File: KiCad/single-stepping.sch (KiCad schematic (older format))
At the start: 8 parts, among them SW1 SW_PUSH_SMALL, U1 4013, U2 74LS00, X1 OSCILLATOR

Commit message: add single-stepped CPU symbol to schema, with LED to blink
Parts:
- added D1: LED, symbol cpu-board-rescue:LED
- added R2: 330, symbol cpu-board-rescue:R
- added U4: 68008D, symbol CPU_NXP_68000:68008D
- gave numbers to parts that had none: 1
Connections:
- net +5V: now also U4.13 (VCC), U4.33 (BR), U4.36 (HALT), U4.37 (RESET), U4.39 (VPA), U4.40 (BERR), U4.41 (IPL1), U4.42 (IPL0/2)
- net DTACK: now also U4.31 (DTACK)
- net GND: now also R2.1, U4.15 (GND), U4.20 (D7), U4.21 (D6), U4.22 (D5), U4.23 (D4), U4.24 (D3), U4.25 (D2), U4.26 (D1), U4.27 (D0), U4.35 (GND)
- net CLK: now reaches U1.11 (C), U1.3 (C), X1.5 (OUT)
- net CLK: now also U4.34 (CLK)
- new net: D1.1 (A), U4.46 (A0)
- new net: D1.2 (K), R2.2
- no-connect marks 3 -> 30

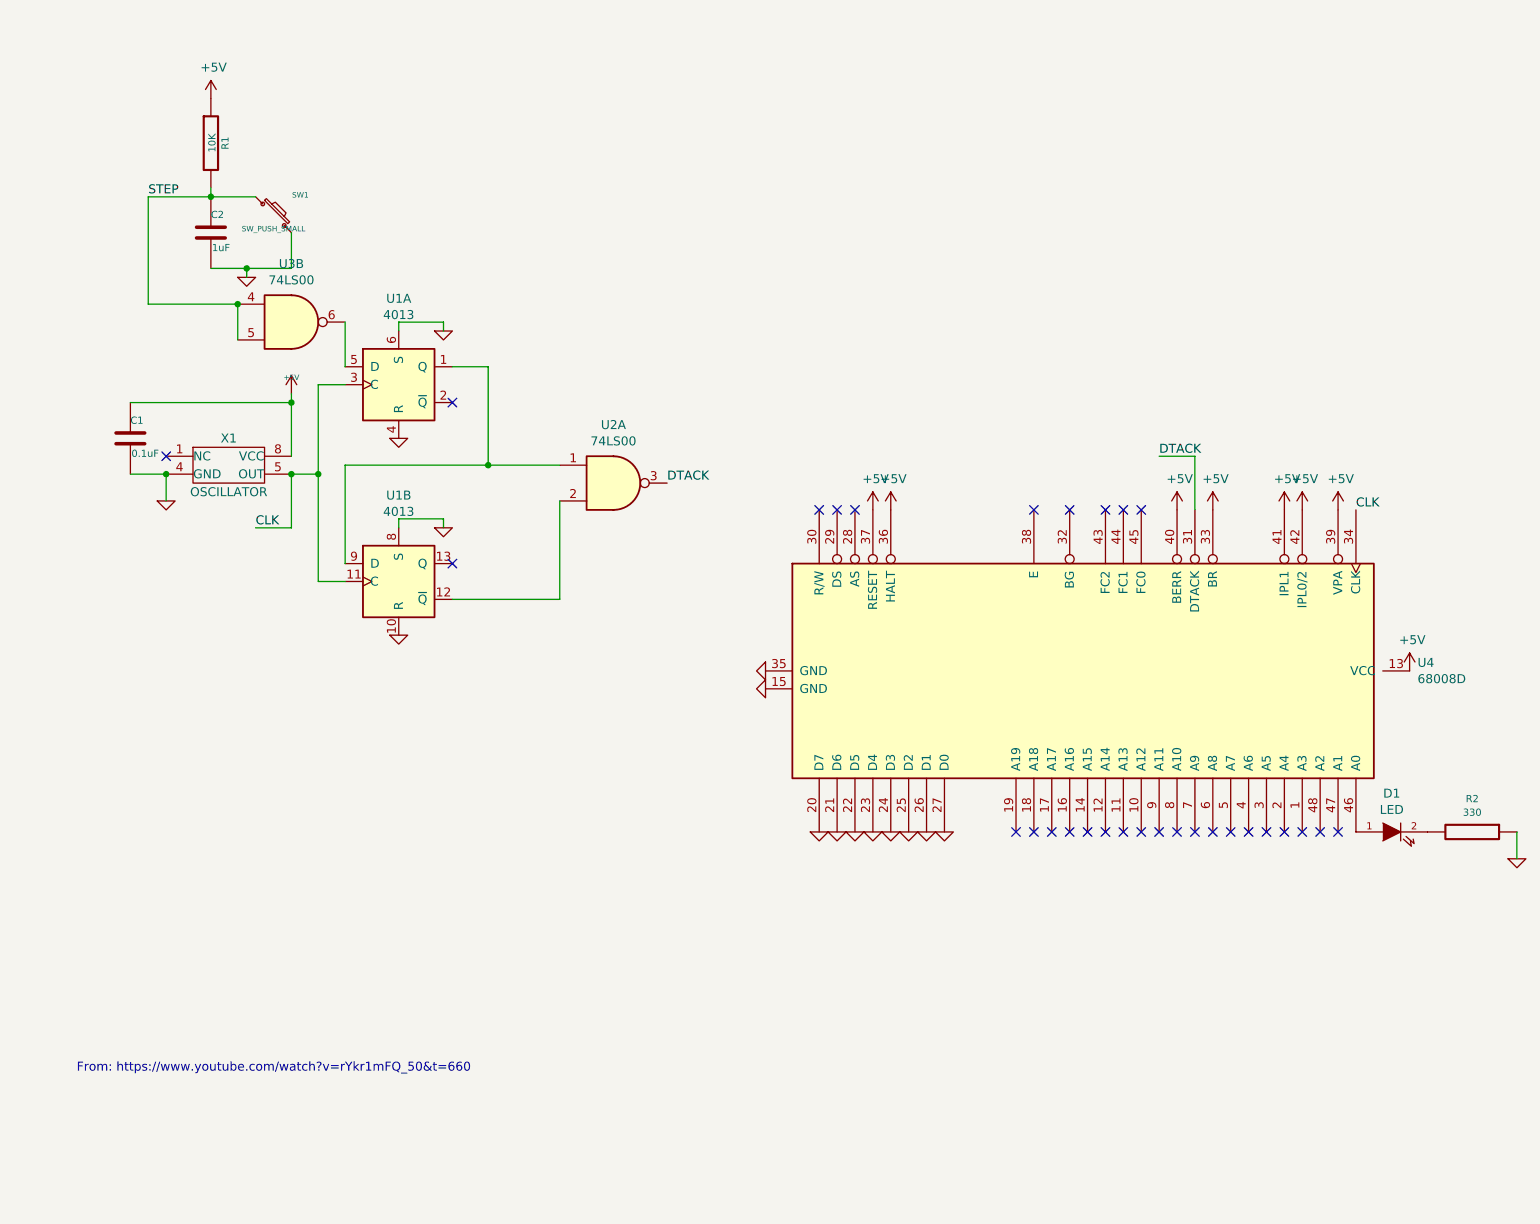
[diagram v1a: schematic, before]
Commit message: fix halt and error line high to pulled high, add power-up reset circuitry
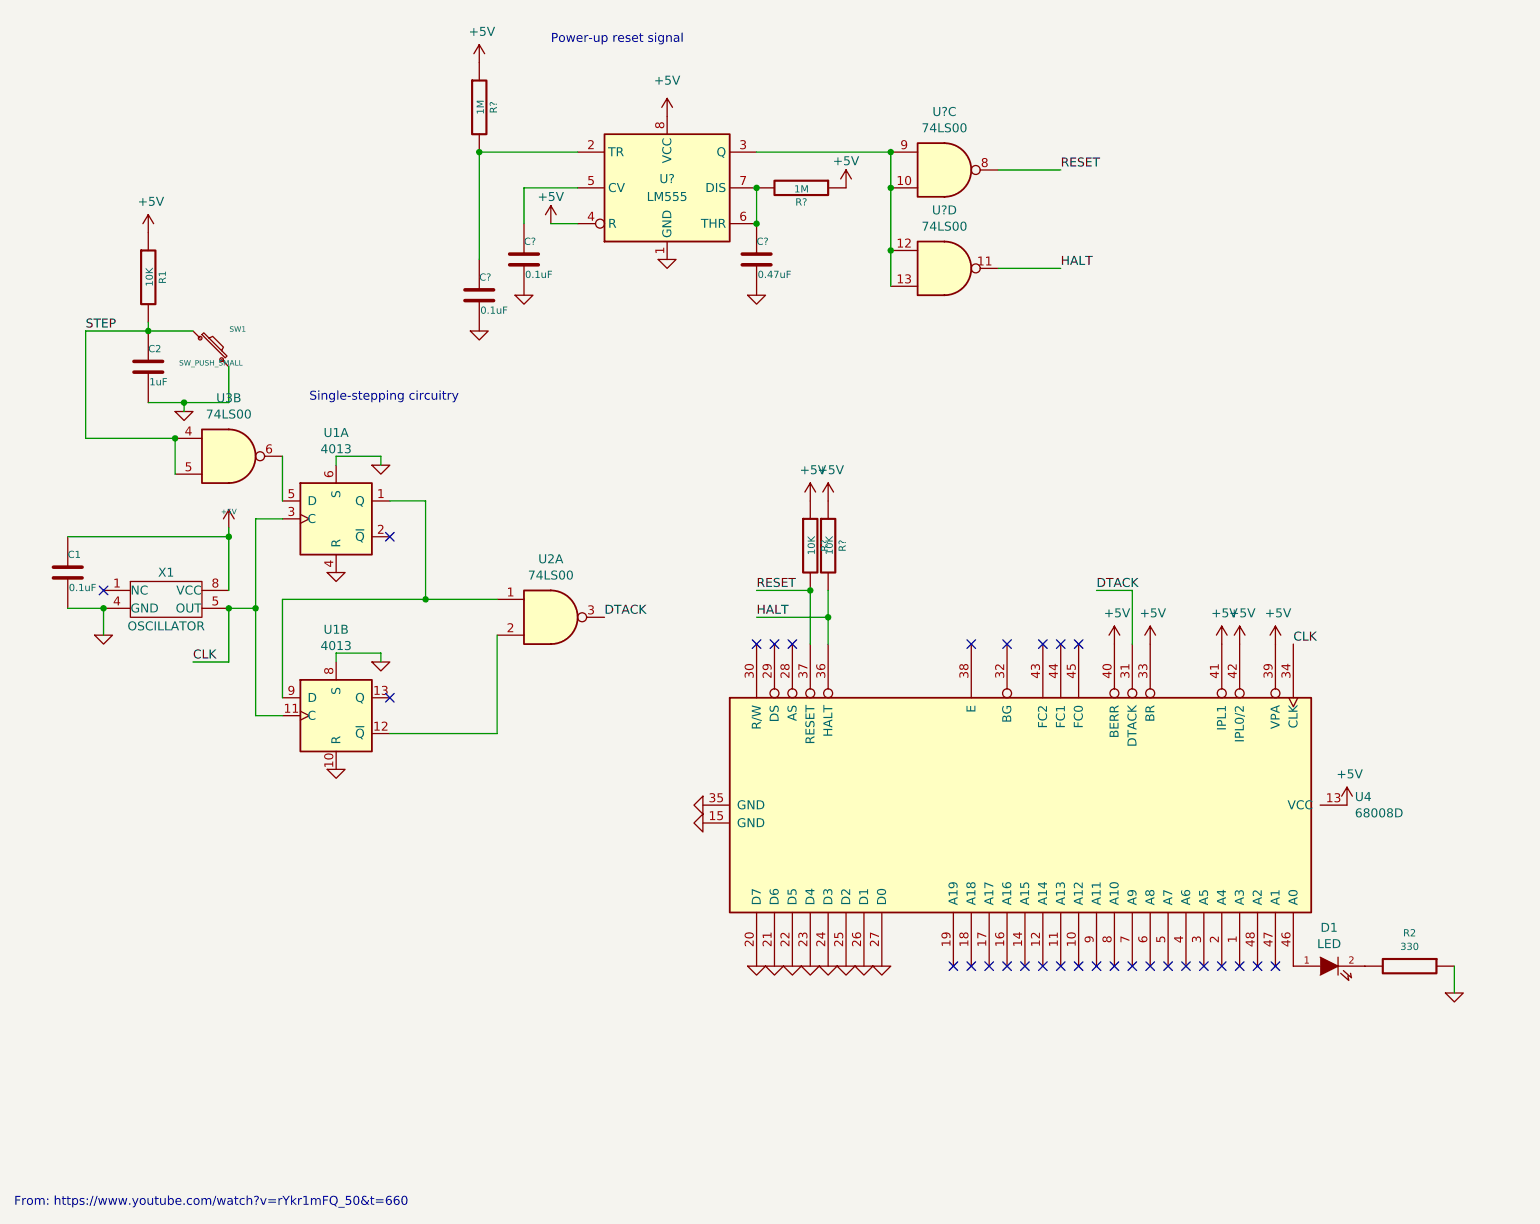
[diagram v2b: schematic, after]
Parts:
- added C? (x2): 0.1uF, Discret:C1, symbol cpu-board-rescue:C
- added C?: 0.47uF, Discret:C1, symbol cpu-board-rescue:C
- added R? (x2): 10K, Discret:R3-5, symbol cpu-board-rescue:R
- added R? (x2): 1M, Discret:R3-5, symbol cpu-board-rescue:R
- added U?: LM555, symbol Timer:LM555
- added U? (x2): 74LS00, symbol 74xx:74LS00
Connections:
- net +5V: now also R?.1, R?.1, R?.1, R?.1, U?.4 (R), U?.8 (VCC); no longer U4.36 (HALT), U4.37 (RESET)
- net GND: now also C?.2, C?.2, C?.2, U?.1 (GND)
- new net: C?.1, R?.2, U?.2 (TR)
- new net: U?.10, U?.12, U?.13, U?.3 (Q), U?.9
- new net: C?.1, U?.5 (CV)
- new net: C?.1, R?.2, U?.6 (THR), U?.7 (DIS)
- new net HALT: R?.2, U4.36 (HALT), U?.11
- new net RESET: R?.2, U4.37 (RESET), U?.8
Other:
- note added: "Power-up reset signal"
- note added: "Single-stepping circuitry"
- moved on the sheet: C1, C2, D1, R1, R2, SW1, U1A, U1B, U2A, U3B, U4, X1

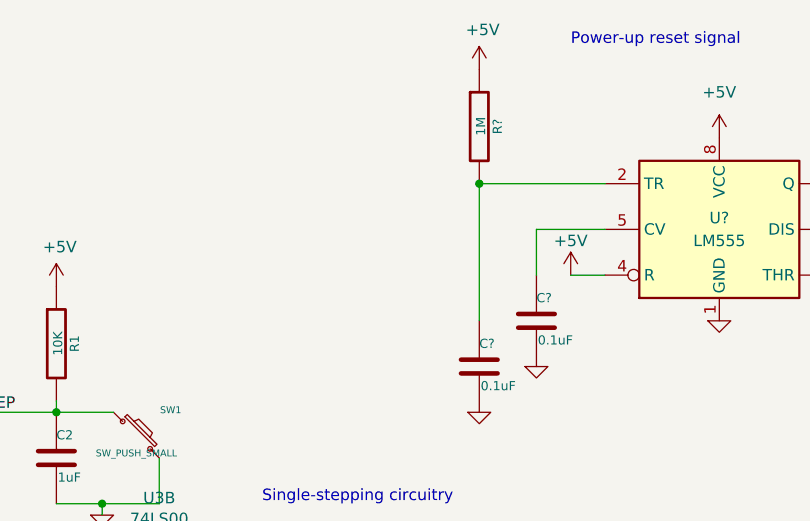
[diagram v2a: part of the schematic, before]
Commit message: Add reset switch
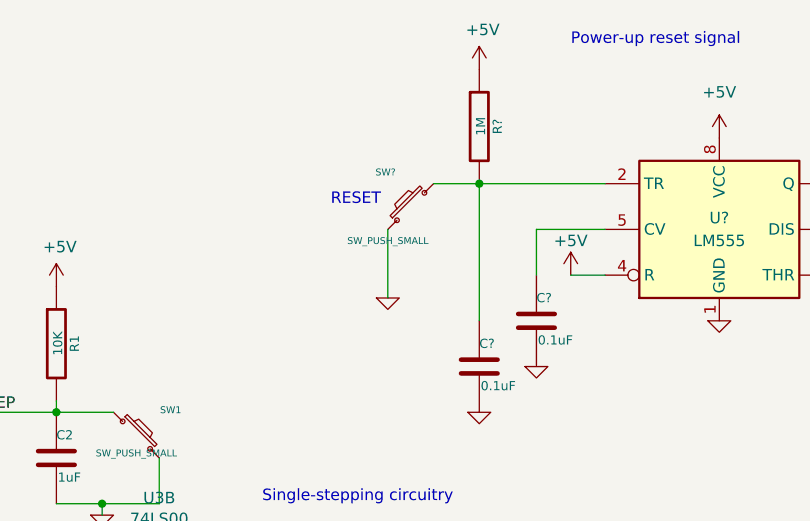
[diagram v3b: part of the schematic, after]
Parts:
- added SW?: SW_PUSH_SMALL, Discret:SW_PUSH_SMALL, symbol cpu-board-rescue:SW_PUSH_SMALL
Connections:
- net GND: now also SW?.1
- net at C?.1, R?.2, U?.2 (TR): now also SW?.2
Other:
- note added: "RESET"
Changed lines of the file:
@@
 Text Notes 2750 2850 0    50   ~ 0
 Single-stepping circuitry
+$Comp
+L cpu-board-rescue:SW_PUSH_SMALL SW?
+U 1 1 5E6E0874
+P 3400 1550
+F 0 "SW?" V 3550 1660 30  0000 C CNN
+F 1 "SW_PUSH_SMALL" V 3250 1650 30  0000 C CNN
+F 2 "Discret:SW_PUSH_SMALL" H 3400 1550 60  0001 C CNN
+F 3 "" H 3400 1550 60  0000 C CNN
+	1    3400 1550
+	0    -1   -1   0
+$EndComp
+Wire Wire Line
+	3500 1450 3700 1450
+Wire Wire Line
+	3300 1650 3300 1950
+$Comp
+L cpu-board-rescue:GND #PWR?
+U 1 1 5E6E4E67
+P 3300 1950
+F 0 "#PWR?" H 3300 1950 30  0001 C CNN
+F 1 "GND" H 3300 1880 30  0001 C CNN
+F 2 "" H 3300 1950 60  0000 C CNN
+F 3 "" H 3300 1950 60  0000 C CNN
+	1    3300 1950
+	1    0    0    -1
+$EndComp
+Text Notes 3050 1550 0    50   ~ 0
+RESET
 $EndSCHEMATC

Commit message: re-order pin configuration, trigger on DTACK
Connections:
- net DTACK renamed ~DTACK
- net HALT renamed ~HALT
- net RESET renamed ~RESET
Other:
- note added: "Power-up reset signal\nAdapted from Jeff Tranter's https://github.com/jefftranter/68000/blob/master/TS2/v2.1/page1.sch"
- note removed: "Power-up reset signal"
- moved on the sheet: C?, R?, SW?
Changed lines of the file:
@@
 NoConn ~ 3200 4500
 Text Label 4400 4050 0    50   ~ 0
-DTACK
+~DTACK
 $Comp
 L cpu-board-rescue:GND #PWR05
@@
 	7350 3900 7150 3900
 Text Label 7150 3900 0    50   ~ 0
-DTACK
+~DTACK
 $Comp
 L power:+5V #PWR023
@@
 	5650 4050 5650 3900
 Text Label 5250 3900 0    50   ~ 0
-RESET
+~RESET
 Text Label 5250 4050 0    50   ~ 0
-HALT
+~HALT
 $Comp
 L Timer:LM555 U?
@@
 L cpu-board-rescue:R R?
 U 1 1 5E6B3594
-P 3700 1200
-F 0 "R?" V 3780 1200 40  0000 C CNN
-F 1 "1M" V 3707 1201 40  0000 C CNN
-F 2 "Discret:R3-5" V 3630 1200 30  0001 C CNN
-F 3 "" H 3700 1200 30  0000 C CNN
-	1    3700 1200
+P 3600 1200
+F 0 "R?" V 3680 1200 40  0000 C CNN
+F 1 "1M" V 3607 1201 40  0000 C CNN
+F 2 "Discret:R3-5" V 3530 1200 30  0001 C CNN
+F 3 "" H 3600 1200 30  0000 C CNN
+	1    3600 1200
 	1    0    0    -1
 $EndComp
@@
 L cpu-board-rescue:C C?
 U 1 1 5E6B3B78
-P 3700 2250
-F 0 "C?" H 3700 2350 40  0000 L CNN
-F 1 "0.1uF" H 3706 2165 40  0000 L CNN
-F 2 "Discret:C1" H 3738 2100 30  0001 C CNN
-F 3 "" H 3700 2250 60  0000 C CNN
-	1    3700 2250
+P 3600 2050
+F 0 "C?" H 3600 2150 40  0000 L CNN
+F 1 "0.1uF" H 3606 1965 40  0000 L CNN
+F 2 "Discret:C1" H 3638 1900 30  0001 C CNN
+F 3 "" H 3600 2050 60  0000 C CNN
+	1    3600 2050
 	1    0    0    -1
 $EndComp
@@
 L power:+5V #PWR?
 U 1 1 5E6B811D
-P 3700 950
-F 0 "#PWR?" H 3700 800 50  0001 C CNN
-F 1 "+5V" H 3715 1123 50  0000 C CNN
-F 2 "" H 3700 950 50  0001 C CNN
-F 3 "" H 3700 950 50  0001 C CNN
-	1    3700 950
+P 3600 950
+F 0 "#PWR?" H 3600 800 50  0001 C CNN
+F 1 "+5V" H 3615 1123 50  0000 C CNN
+F 2 "" H 3600 950 50  0001 C CNN
+F 3 "" H 3600 950 50  0001 C CNN
+	1    3600 950
 	1    0    0    -1
 $EndComp
@@
 	1    0    0    -1
 $EndComp
-Wire Wire Line
-	3700 1450 4250 1450
-Wire Wire Line
-	3700 1450 3700 2050
-Connection ~ 3700 1450
 $Comp
 L cpu-board-rescue:GND #PWR?
 U 1 1 5E6BEF9F
-P 3700 2450
-F 0 "#PWR?" H 3700 2450 30  0001 C CNN
-F 1 "GND" H 3700 2380 30  0001 C CNN
-F 2 "" H 3700 2450 60  0000 C CNN
-F 3 "" H 3700 2450 60  0000 C CNN
-	1    3700 2450
+P 3600 2250
+F 0 "#PWR?" H 3600 2250 30  0001 C CNN
+F 1 "GND" H 3600 2180 30  0001 C CNN
+F 2 "" H 3600 2250 60  0000 C CNN
+F 3 "" H 3600 2250 60  0000 C CNN
+	1    3600 2250
 	1    0    0    -1
 $EndComp
@@
 $EndComp
 Text Label 6950 1550 0    50   ~ 0
-RESET
+~RESET
 Text Label 6950 2100 0    50   ~ 0
-HALT
+~HALT
 Text Notes 4100 850  0    50   ~ 0
-Power-up reset signal
+Power-up reset signal\nAdapted from Jeff Tranter's https://github.com/jefftranter/68000/blob/master/TS2/v2.1/page1.sch
 Text Notes 2750 2850 0    50   ~ 0
 Single-stepping circuitry
@@
 L cpu-board-rescue:SW_PUSH_SMALL SW?
 U 1 1 5E6E0874
-P 3400 1550
-F 0 "SW?" V 3550 1660 30  0000 C CNN
-F 1 "SW_PUSH_SMALL" V 3250 1650 30  0000 C CNN
-F 2 "Discret:SW_PUSH_SMALL" H 3400 1550 60  0001 C CNN
-F 3 "" H 3400 1550 60  0000 C CNN
-	1    3400 1550
+P 3350 1550
+F 0 "SW?" V 3500 1660 30  0000 C CNN
+F 1 "SW_PUSH_SMALL" V 3200 1650 30  0000 C CNN
+F 2 "Discret:SW_PUSH_SMALL" H 3350 1550 60  0001 C CNN
+F 3 "" H 3350 1550 60  0000 C CNN
+	1    3350 1550
 	0    -1   -1   0
 $EndComp
-Wire Wire Line
-	3500 1450 3700 1450
-Wire Wire Line
-	3300 1650 3300 1950
 $Comp
 L cpu-board-rescue:GND #PWR?
 U 1 1 5E6E4E67
-P 3300 1950
-F 0 "#PWR?" H 3300 1950 30  0001 C CNN
-F 1 "GND" H 3300 1880 30  0001 C CNN
-F 2 "" H 3300 1950 60  0000 C CNN
-F 3 "" H 3300 1950 60  0000 C CNN
-	1    3300 1950
+P 3250 2250
+F 0 "#PWR?" H 3250 2250 30  0001 C CNN
+F 1 "GND" H 3250 2180 30  0001 C CNN
+F 2 "" H 3250 2250 60  0000 C CNN
+F 3 "" H 3250 2250 60  0000 C CNN
+	1    3250 2250
 	1    0    0    -1
 $EndComp
 Text Notes 3050 1550 0    50   ~ 0
 RESET
+Wire Wire Line
+	3250 1650 3250 2250
+Wire Wire Line
+	3450 1450 3600 1450
+Wire Wire Line
+	3600 1850 3600 1450
+Connection ~ 3600 1450
+Wire Wire Line
+	3600 1450 4250 1450
 $EndSCHEMATC
